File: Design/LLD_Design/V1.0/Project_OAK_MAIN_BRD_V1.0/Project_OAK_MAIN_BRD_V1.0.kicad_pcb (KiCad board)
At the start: 6 copper layers, 42.6 x 42.6 mm, 113 parts, among them U1 ATmega328PB-MU, U2 RV-8263-C7-32.768KHZ-20PPM-TA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, U3 LIS2DW12TR

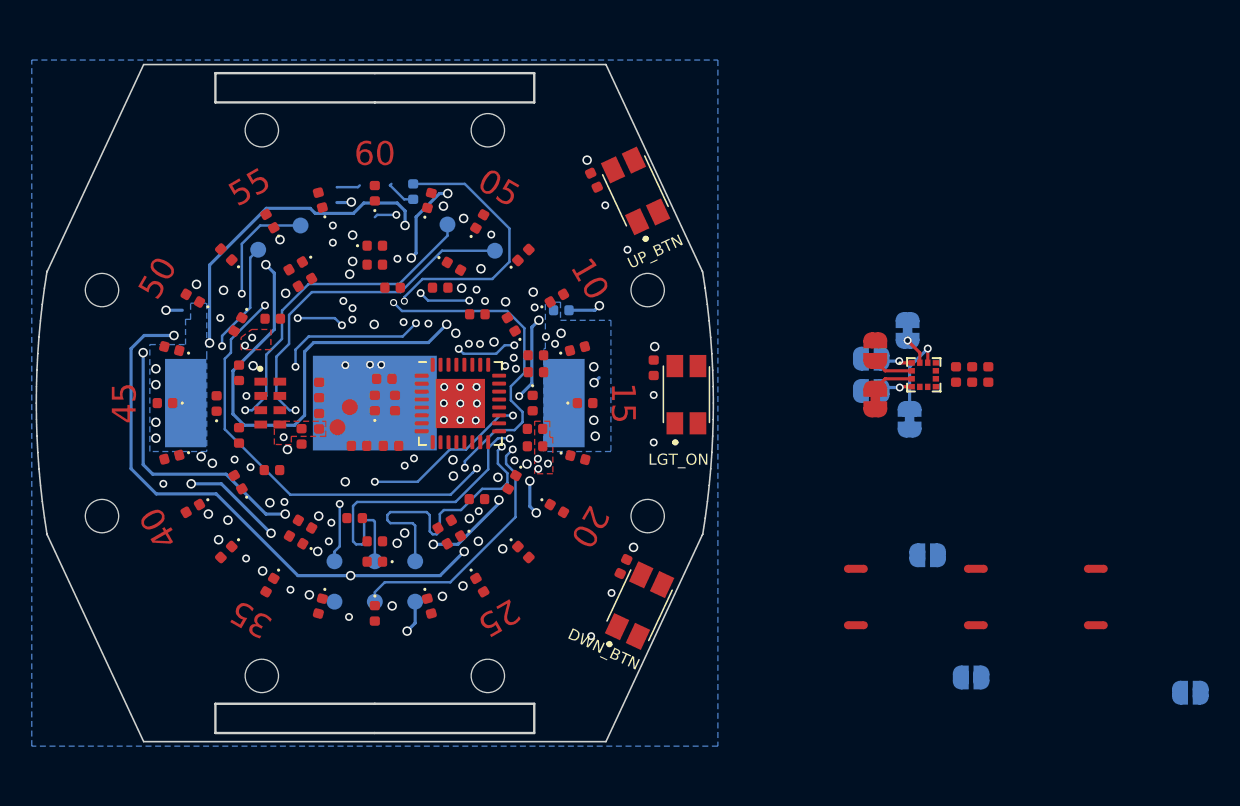
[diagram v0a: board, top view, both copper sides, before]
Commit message: updated main board
changed main board stack up from 6L to 4L, updated schematics with symbol & footprint change for push button and updated main board outline with latest mechanical changes.
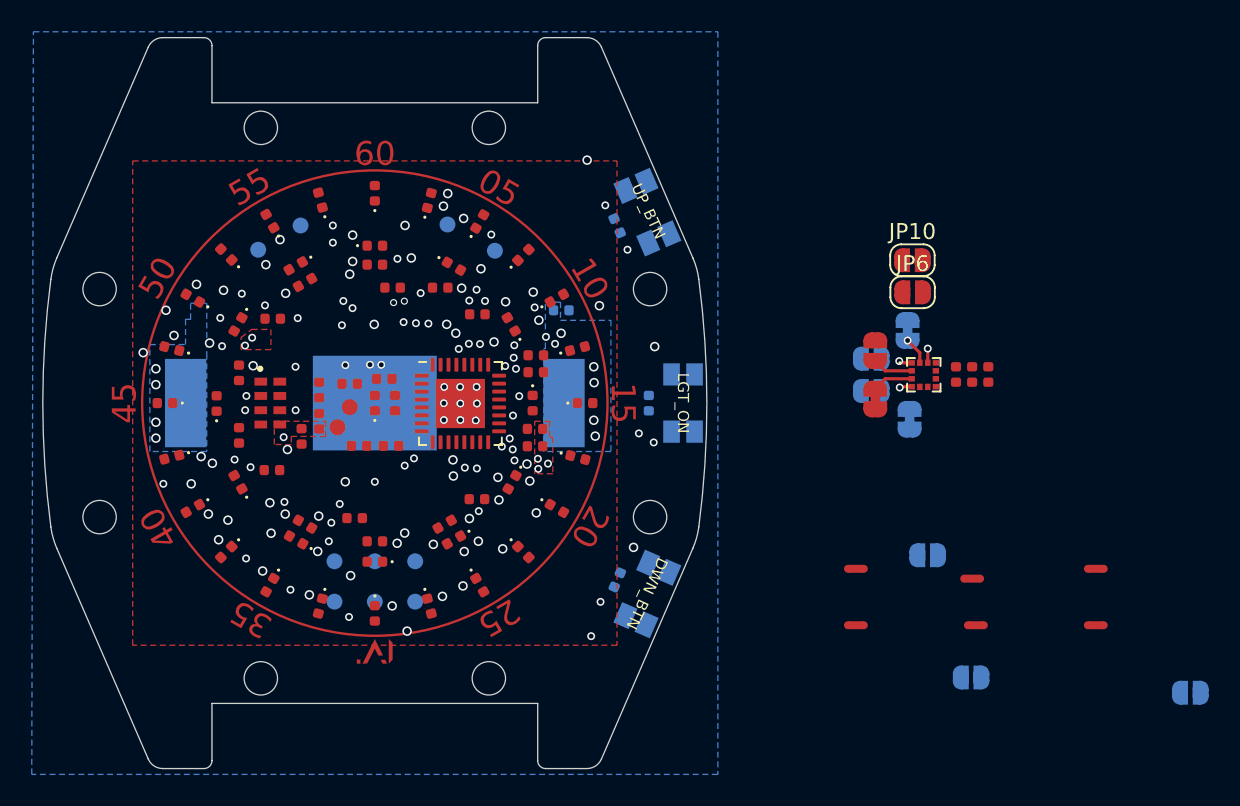
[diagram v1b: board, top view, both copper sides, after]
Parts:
- removed the REF** at (87.6, 86.4)
- removed the REF** at (87.6, 100.6)
- removed the REF** at (77.6, 110.6)
- removed the REF** at (63.3, 110.6)
- removed the REF** at (53.3, 100.6)
- removed the REF** at (53.3, 86.4)
- removed the REF** at (63.3, 76.3)
- removed the REF** at (77.6, 76.3)
- added G***: LOGO, AI_logo:AI_logo_v1, F.Cu at (70.5, 109.4)
- added JP10: SolderJumper_2_Open, Jumper:SolderJumper-2_P1.3mm_Open_RoundedPad1.0x1.5mm, F.Cu at (104.3, 84.5)
- added JP6: SolderJumper_2_Open, Jumper:SolderJumper-2_P1.3mm_Open_RoundedPad1.0x1.5mm, F.Cu at (104.3, 86.5)
- added REF**: ., MountingHole:MountingHole_2.1mm, F.Cu at (63.3, 76.1)
- added REF**: ., MountingHole:MountingHole_2.1mm, F.Cu at (53.1, 86.3)
- added REF**: ., MountingHole:MountingHole_2.1mm, F.Cu at (53.1, 100.6)
- added REF**: ., MountingHole:MountingHole_2.1mm, F.Cu at (63.3, 110.8)
- added REF**: ., MountingHole:MountingHole_2.1mm, F.Cu at (77.6, 110.8)
- added REF**: ., MountingHole:MountingHole_2.1mm, F.Cu at (87.8, 100.6)
- added REF**: ., MountingHole:MountingHole_2.1mm, F.Cu at (87.8, 86.3)
- added REF**: ., MountingHole:MountingHole_2.1mm, F.Cu at (77.6, 76.1)
- C1, C2, C3: moved to B.Cu
- R6: moved to F.Cu
- S1, S2, S3: footprint Button_Switch_SMD:EVQP7J01P -> Button_Switch_SMD:SW_EVQ-P7A01P; moved to B.Cu
- moved R6 12.7 mm to (68.9, 92.3), turned to 180 degrees
- moved C2 3.22 mm to (85.7, 82.3), turned to 293.5 degrees
- moved C1 2.25 mm to (87.7, 93.5)
- moved S2 1.23 mm to (87.6, 81.5), turned to 293.5 degrees
- moved S3 1.18 mm to (87.6, 105.5), turned to 246.5 degrees
- moved C3 0.93 mm to (85.7, 104.6), turned to 246.5 degrees
- moved NT5 0.66 mm to (108.1, 104.5)
- moved S1 0.31 mm to (89.9, 93.5), turned to 270 degrees
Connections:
- net Net-(D1-Pad2) renamed /MON_LED_R
- net Net-(JP1-Pad2) renamed /ACC_CS
- net Net-(JP2-Pad2) renamed /ACC_SDA0
- JP5 pad 1: /LGT_ON_BTN -> /PE1
- R14 pad 2: /VOL_MON -> /V_MON
- R15 pad 1: /VOL_MON -> /V_MON
- U1 pad 19: /VOL_MON -> /PE2
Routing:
- net Net-(S1-Pad2): track 0.00 -> 50.8 mm, vias 0 -> 2
- net /LGT_ON_BTN: track 50.8 -> 0.00 mm, vias 2 -> 0
- net /EXT_3V3_IN: track 36.6 -> 0.00 mm
- net /R6: track 35.0 -> 0.00 mm
- net /R3_R: track 45.2 -> 15.8 mm
- net /C2: track 27.1 -> 0.00 mm
- net /RTC_CLKO: track 21.7 -> 0.00 mm
- net /RTC_CLKO_EN: track 20.6 -> 0.00 mm
- net /C1: track 20.5 -> 0.00 mm
- net /R2_R: track 40.3 -> 20.1 mm
- net /ICSP_SCK: track 20.0 -> 0.00 mm
- net /ICSP_MISO: track 17.9 -> 0.00 mm
- net /C6_T: track 17.3 -> 0.00 mm
- net /MON_LED: track 17.1 -> 0.00 mm
- net /ICSP_MOSI: track 16.1 -> 0.00 mm
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- removed copper zone on In4.Cu, net +3V0
- removed copper zone on In1.Cu, net GND
- removed copper zone on In3.Cu, net GND
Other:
- board size 42.6 x 42.6 mm -> 41.8 x 46 mm
- copper layers 6 -> 4
- net class Power: trace_width 0.2 -> 0.25
- net class Signal: trace_width 0.156 -> 0.242
- board text added: "X: 53.136859 Y: 100.647314"
- board text added: "X: 53.136859 Y: 86.296686"
- board text added: "X: 63.284286 Y: 100.794741"
- board text added: "X: 63.284286 Y: 76.149259"
- board text added: "X: 77.634914 Y: 100.794741"
- board text added: "X: 77.634914 Y: 76.149259"
- board text added: "X: 87.61222 Y: 105.4862 angle: 246.5"
- board text added: "X: 87.61222 Y: 81.45526 angle: 293.5"
- board text added: "X: 87.782341 Y: 100.647314"
- board text added: "X: 87.782341 Y: 86.296686"
- board text added: "X: 89.85758 Y: 93.46946 angle: 270"

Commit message: Updated placement
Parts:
- removed JP3, JP4: SolderJumper_2_Bridged, Jumper:SolderJumper-2_P1.3mm_Bridged_RoundedPad1.0x1.5mm
- removed the JP6 at (104.1, 94.5)
- removed the JP6 at (104.3, 86.5)
- removed JP7, JP8: SolderJumper_2_Open, Jumper:SolderJumper-2_P1.3mm_Open_RoundedPad1.0x1.5mm
- removed TP10, TP8, TP9: TestPoint, TestPoint:TestPoint_Pad_D1.0mm
- added JP6: SolderJumper_2_Open, Jumper:SolderJumper-2_Open_Pad1.0x1.5mm_custom, F.Cu at (72.4, 98.0)
- JP1: footprint Jumper:SolderJumper-2_P1.3mm_Open_RoundedPad1.0x1.5mm -> Jumper:SolderJumper-2_Open_Pad1.0x1.5mm_custom; moved to B.Cu
- JP10, JP9: footprint Jumper:SolderJumper-2_P1.3mm_Open_RoundedPad1.0x1.5mm -> Jumper:SolderJumper-2_Open_Pad1.0x1.5mm_custom
- JP2: footprint Jumper:SolderJumper-2_P1.3mm_Bridged_RoundedPad1.0x1.5mm -> Jumper:SolderJumper-2_Bridged_Pad1.0x1.5mm_custom; moved to B.Cu
- JP5: footprint Jumper:SolderJumper-2_P1.3mm_Bridged_RoundedPad1.0x1.5mm -> Jumper:SolderJumper-2_Bridged_Pad1.0x1.5mm_custom
- NT1, NT2, NT3, NT4, NT5, NT6: footprint NetTie:NetTie-2_SMD_Pad0.5mm -> NetTie:NetTie-2_SMD_Custom
- TP11: moved to F.Cu
- moved NT4 44.0 mm to (74.3, 89.5), turned to 90 degrees
- moved NT1 41.8 mm to (78.1, 89.5), turned to 270 degrees
- moved C11 41.6 mm to (67.6, 88.3), turned to 90 degrees
- moved JP9 39.8 mm to (84.6, 97.5), turned to 90 degrees
- moved C5 39.6 mm to (68.6, 88.3), turned to 90 degrees
- moved C10 39.0 mm to (68.1, 89.8), turned to 180 degrees
- moved JP10 38.2 mm to (68.5, 98.0), turned to 90 degrees
- moved JP5 36.2 mm to (68.9, 79.9)
- moved NT2 36.0 mm to (77.1, 89.5), turned to 90 degrees
- moved U3 34.7 mm to (70.5, 88.6), turned to 180 degrees
- moved NT5 34.4 mm to (74.4, 97.5), turned to 270 degrees
- moved JP2 34.2 mm to (70.5, 79.9), turned to 270 degrees
- moved JP1 31.7 mm to (72.0, 79.9)
- moved NT3 31.3 mm to (75.1, 89.5), turned to 90 degrees
- moved NT6 26.3 mm to (75.2, 97.5), turned to 270 degrees
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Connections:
- U3 pad 1: /A_SCL -> /SNS_SCL
- U3 pad 4: /A_SDA -> /SNS_SDA
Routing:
- net GND: track 0.00 -> 99.8 mm, vias 44 -> 35
- net /DWN_BTN: track 70.8 -> 3.35 mm, vias 2 -> 1
- net /R3: track 65.2 -> 100.7 mm, vias 5 -> 6
- net /UP_BTN: track 33.0 -> 4.76 mm, vias 2 -> 1
- net +3V0: track 0.00 -> 23.1 mm, vias 23 -> 16
- net /SNS_SCL: track 10.7 -> 28.8 mm, vias 2 -> 0
- net /SNS_SDA: track 11.7 -> 20.9 mm, vias 2 -> 0
- net /MON_LED: track 0.00 -> 7.56 mm, vias 1 -> 2
- net /R2_R: track 20.1 -> 13.0 mm, vias 3 -> 1
- net /PE2: track 0.00 -> 5.57 mm, vias 0 -> 1
- net /R5: track 44.1 -> 49.6 mm, vias 7 -> 9
- net /PB7: track 0.00 -> 5.42 mm
- net /C6: track 25.4 -> 20.1 mm, vias 2 -> 1
- net /ACC_INT2: track 0.89 -> 5.52 mm, vias 1 -> 2
- net /R6_R: track 0.00 -> 4.61 mm
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- removed copper zone on F.Cu, net +3V0
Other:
- net class Power: trace_width 0.25 -> 0.2; via_dia 0.6 -> 0.45; via_drill 0.4 -> 0.3
- net class Signal: trace_width 0.242 -> 0.1565; via_dia 0.5 -> 0.45

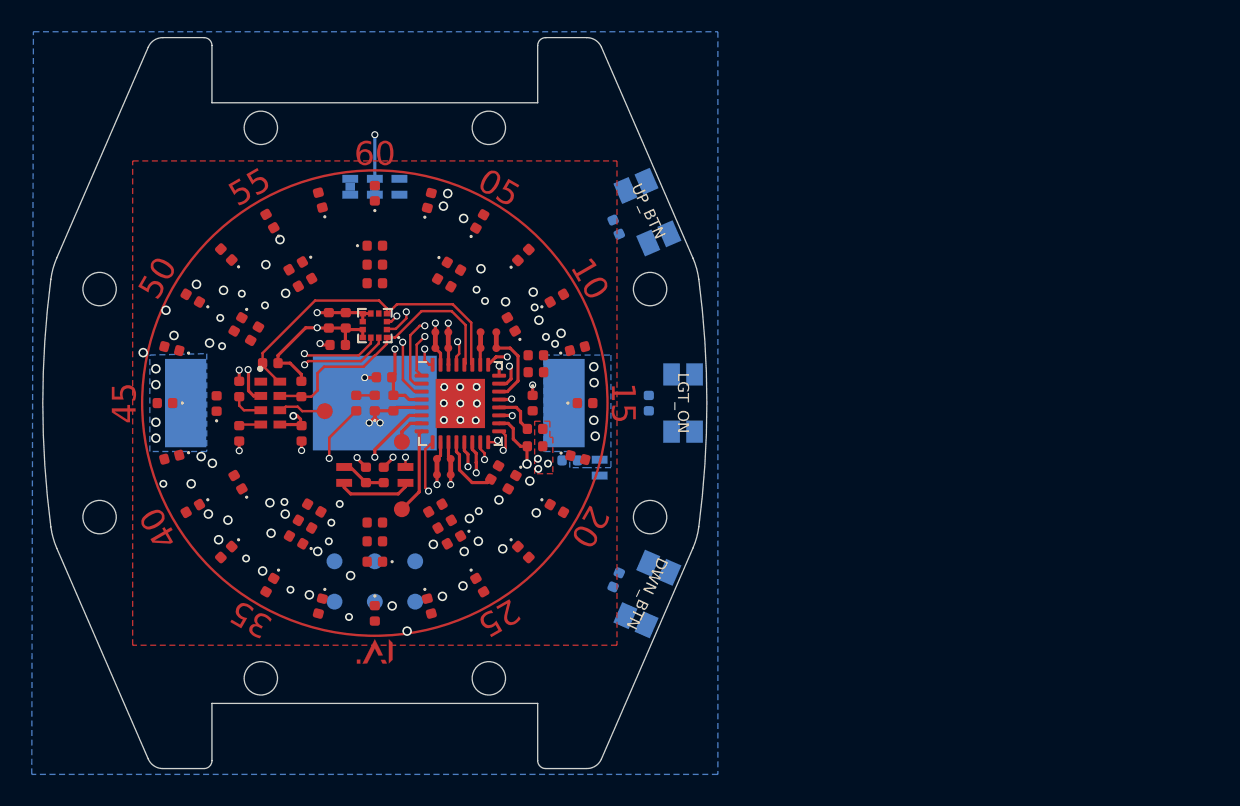
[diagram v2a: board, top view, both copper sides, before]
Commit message: updated layout
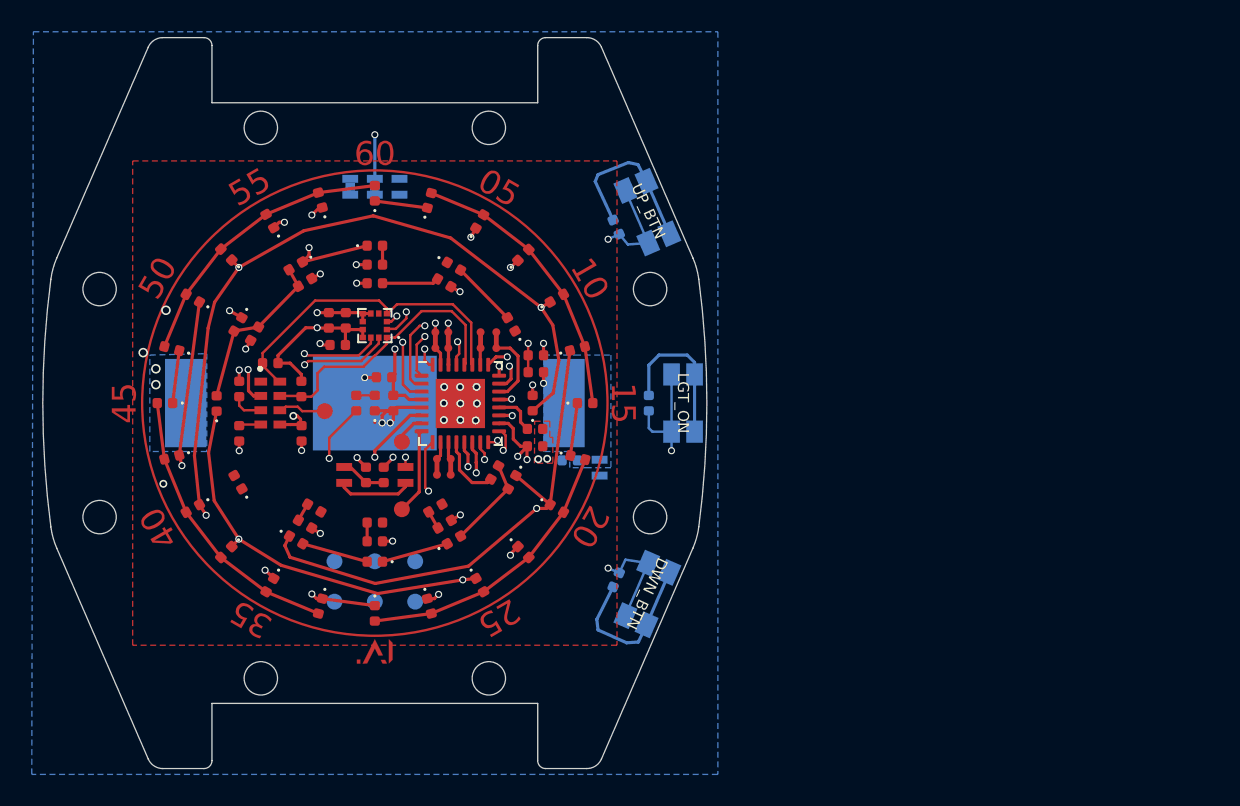
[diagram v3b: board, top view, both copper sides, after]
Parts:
- turned C2 to 113.5 degrees
- turned D20 to 90 degrees
- turned D27 to 330 degrees
- turned D32 to 30 degrees
- turned R23 to 60 degrees
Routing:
- net Net-(S1-Pad2): track 54.2 -> 0.00 mm
- net GND: track 99.8 -> 53.9 mm, vias 35 -> 30
- net /R3: track 100.7 -> 66.7 mm, vias 6 -> 5
- net /R5: track 49.6 -> 74.8 mm, vias 9 -> 2
- net /C3_T: track 0.00 -> 21.4 mm, vias 1 -> 0
- net /C5_T: track 0.00 -> 19.1 mm
- net /C4_T: track 0.00 -> 19.1 mm
- net /C6_T: track 0.00 -> 19.1 mm, vias 2 -> 1
- net /C6: track 20.1 -> 1.40 mm
- net /C5: track 18.9 -> 0.61 mm, vias 2 -> 1
- net /R5_R: track 17.5 -> 1.11 mm, vias 1 -> 0
- net /R3_R: track 17.0 -> 1.18 mm, vias 2 -> 0
- net /R4: track 55.4 -> 70.4 mm, vias 6 -> 4
- net /R1: track 54.8 -> 40.0 mm, vias 4 -> 2
- net /C2_T: track 0.00 -> 14.8 mm
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- added copper zone on In1.Cu, net GND

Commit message: layout update
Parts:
- turned C18 to 180 degrees
- turned D20 to 270 degrees
- turned D8 to 150 degrees
- turned JP5 to 90 degrees
- turned R18 to 0 degrees
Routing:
- net /R6: track 10.9 -> 74.7 mm, vias 0 -> 5
- net /C3: track 2.69 -> 34.2 mm
- net /PE1: track 4.28 -> 29.3 mm
- net /MCU_RSTn: track 3.38 -> 27.5 mm
- net /C6: track 1.40 -> 23.4 mm, vias 1 -> 2
- net /C1_T: track 11.8 -> 33.6 mm, vias 1 -> 6
- net /C2: track 2.26 -> 23.4 mm
- net /C5: track 0.61 -> 19.8 mm, vias 1 -> 2
- net /RTC_INTO: track 4.19 -> 22.9 mm, vias 1 -> 2
- net /ACC_INT2: track 5.52 -> 22.7 mm
- net /LGT_ON_BTN: track 8.73 -> 25.4 mm, vias 2 -> 1
- net /C6_T: track 19.1 -> 35.6 mm, vias 1 -> 2
- net /C4: track 1.72 -> 18.0 mm, vias 1 -> 2
- net /UP_BTN: track 11.3 -> 27.3 mm, vias 2 -> 1
- net /R4: track 70.4 -> 86.0 mm, vias 4 -> 5
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- added copper zone on In2.Cu, net +3V0
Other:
- net class Power: clearance 0.2 -> 0.15
- net class Signal: clearance 0.2 -> 0.15

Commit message: update layout
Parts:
- added BT1: BC-2018-TR, Battery:BAT_BC-2018-TR, B.Cu at (70.5, 93.5)
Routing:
- net +3V0: track 29.3 -> 125.4 mm, vias 14 -> 13
- net GND: track 56.1 -> 51.6 mm, vias 28 -> 64
- net /ACC_INT2: track 22.7 -> 24.2 mm
- net /PE1: track 29.3 -> 30.7 mm
- net /RTC_INTO: track 22.9 -> 21.6 mm
- net /R4: track 86.0 -> 85.8 mm, vias 5 -> 6
- added copper zone on In2.Cu, net GND
- removed copper zone on In2.Cu, net +3V0
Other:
- net class Default: clearance 0.2 -> 0.15; via_dia 0.6 -> 0.45; via_drill 0.4 -> 0.3
- rule trace_clearance: 0.2 -> 0.15

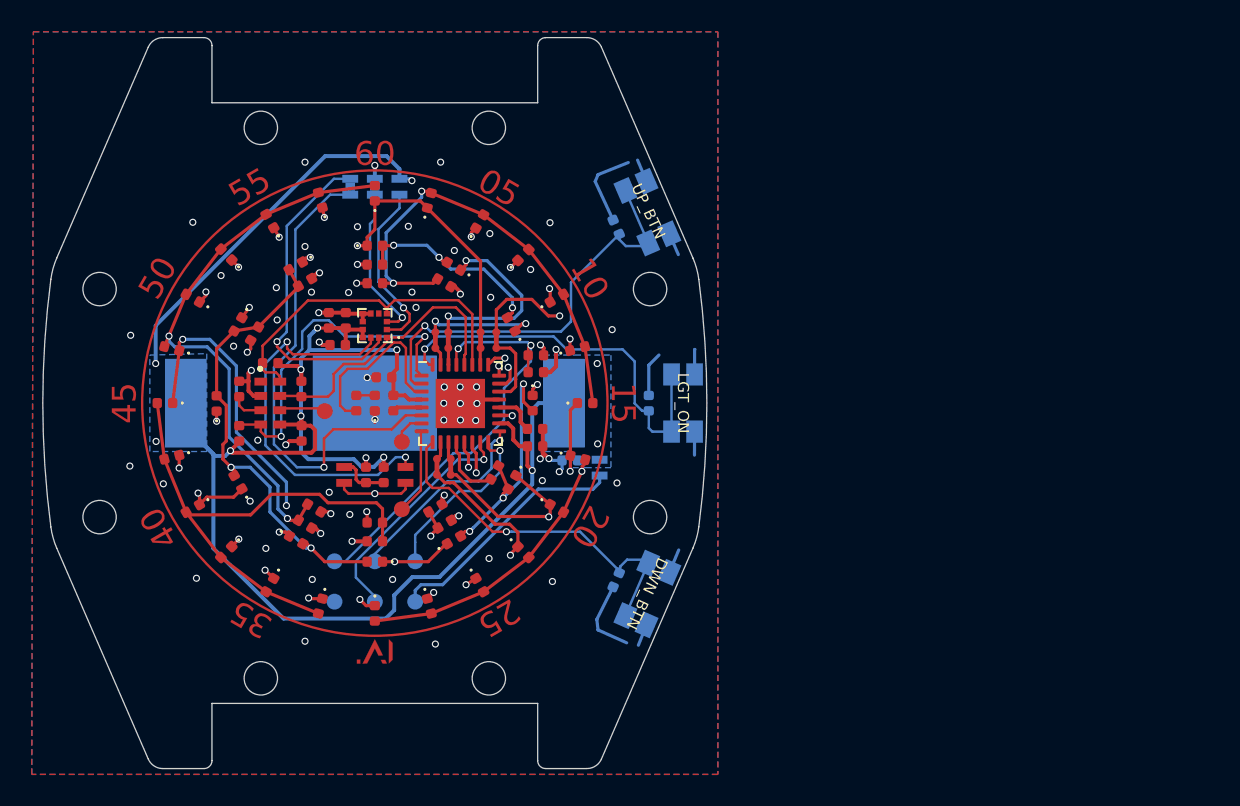
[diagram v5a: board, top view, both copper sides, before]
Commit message: removed thermal vias from MCU
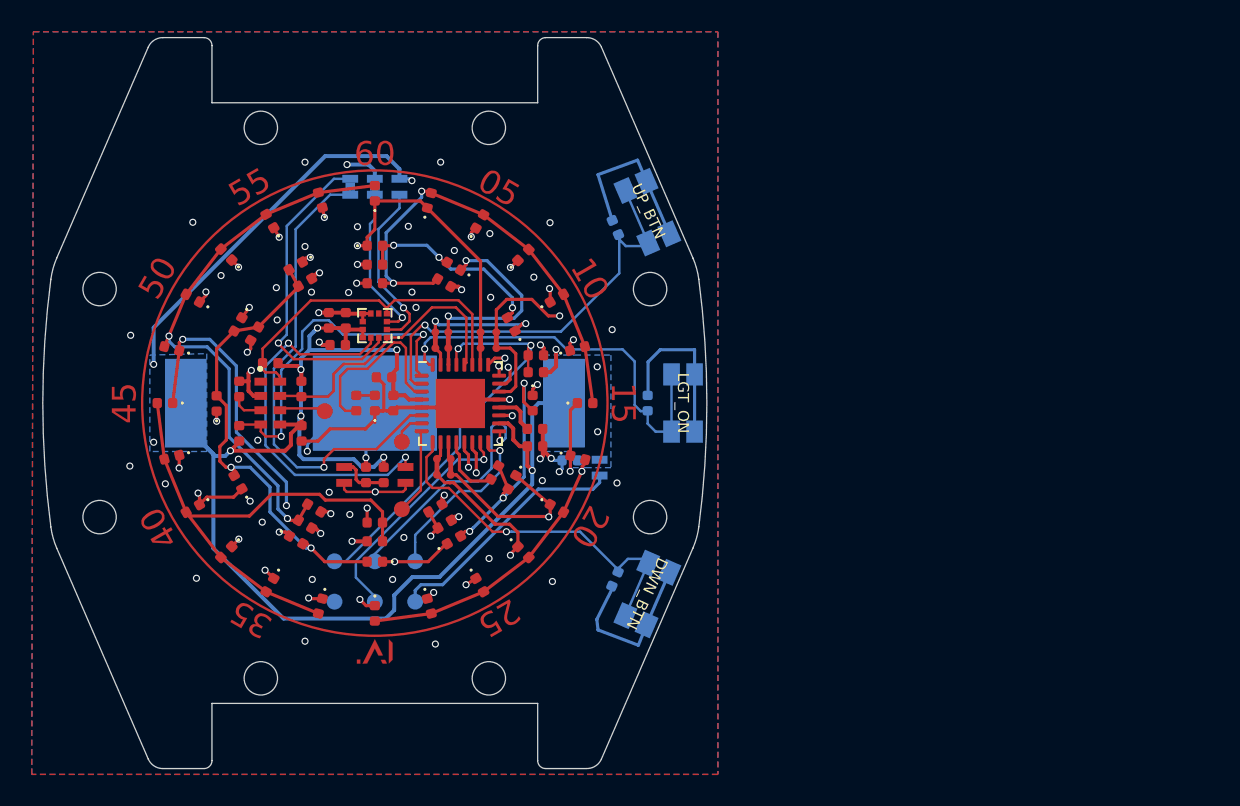
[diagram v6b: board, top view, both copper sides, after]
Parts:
- moved C3 0.09 mm to (85.6, 104.5)
- moved C1 0.07 mm to (87.6, 93.5)
- moved C2 0.06 mm to (85.6, 82.4)
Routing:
- net GND: track 51.6 -> 83.4 mm, vias 64 -> 56
- net /ICSP_SCK: track 12.8 -> 15.4 mm
- net +3V0: track 125.4 -> 123.7 mm
- net /PE1: track 30.7 -> 30.0 mm
- net /MCU_RSTn: track 27.4 -> 26.7 mm
- net /R4: track 85.8 -> 86.1 mm, vias 6 -> 5

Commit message: added Gerber files
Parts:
- moved C4 2.11 mm to (82.7, 99.2)
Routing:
- net GND: track 83.4 -> 82.4 mm, vias 56 -> 55
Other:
- board text added: "ck"
- board text added: "rst"
- board text added: "si"
- board text added: "so"

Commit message: added V1.0 BOM, updated greber
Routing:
- net /MON_LED: track 11.6 -> 10.5 mm
- net /MCU_RSTn: track 26.7 -> 27.4 mm
- net /SNS_SCL: track 18.2 -> 17.5 mm
- net GND: track 82.4 -> 82.7 mm, vias 55 -> 66
